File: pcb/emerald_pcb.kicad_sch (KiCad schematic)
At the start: 34 parts, among them J1 SIM_Card, J2 USB_B_Mini, J3 LiPoBatteryConnector, SW1 ESP RESET, U1 ESP32-S3-MINI-1U, U2 SIM800C, U3 SX1278, U4 MPU-6050, U5 FXMA108, U6 CH340N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

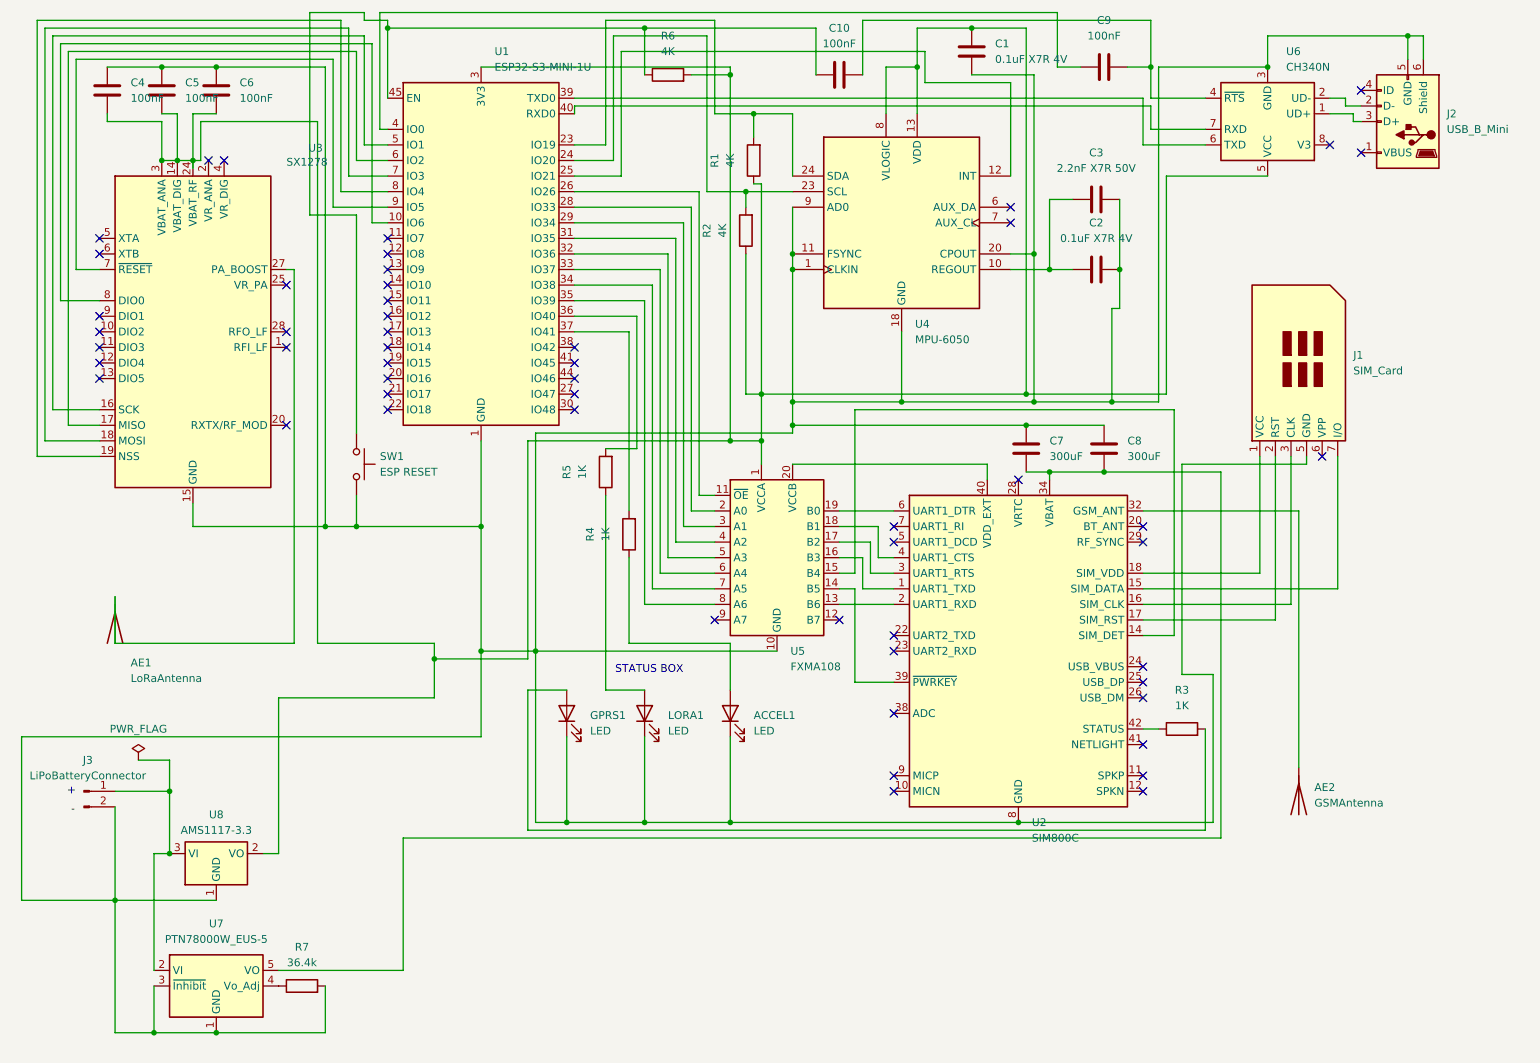
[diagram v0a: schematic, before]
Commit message: feat: update to version 1.1
Changed power inputs, various schematic changes, added decoupling capacitors, removed rare components
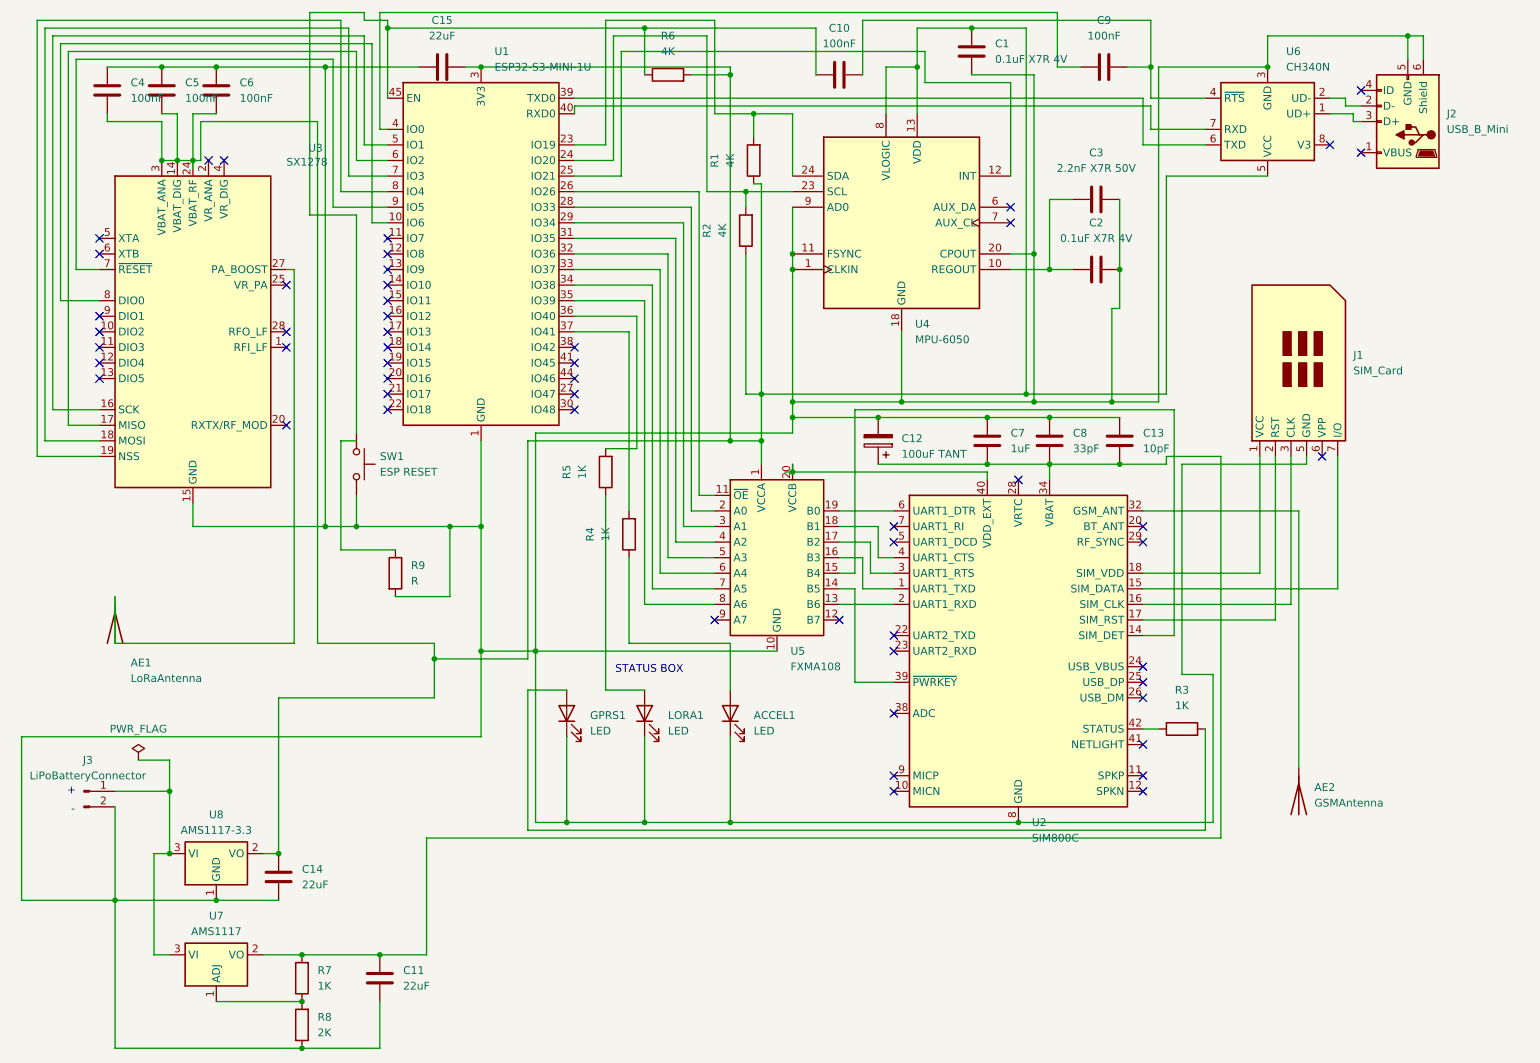
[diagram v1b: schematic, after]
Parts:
- removed U7: PTN78000W_EUS-5, Module:Texas_EUS_R-PDSS-T5_THT, symbol Converter_DCDC:PTN78000W_EUS-5
- added C11, C14, C15: 22uF, Capacitor_SMD:C_0201_0603Metric, symbol Device:C
- added C12: 100uF TANT, Capacitor_SMD:C_0201_0603Metric, symbol Device:C_Polarized
- added C13: 10pF, Capacitor_SMD:C_0201_0603Metric, symbol Device:C
- added R8: 2K, Resistor_SMD:R_0201_0603Metric, symbol Device:R
- added R9: R, symbol Device:R
- added U7: AMS1117, Package_TO_SOT_SMD:SOT-223-3_TabPin2, symbol Regulator_Linear:AMS1117
- C1, C2, C3: footprint Capacitor_SMD:CP_Elec_3x5.3 -> Capacitor_SMD:C_0201_0603Metric
- C10, C4, C5, C6, C9: footprint Capacitor_SMD:CP_Elec_4x3 -> Capacitor_SMD:C_0201_0603Metric
- C7: value 300uF -> 1uF; footprint Capacitor_SMD:CP_Elec_4x3 -> Capacitor_SMD:C_0201_0603Metric
- C8: value 300uF -> 33pF; footprint Capacitor_SMD:CP_Elec_4x3 -> Capacitor_SMD:C_0201_0603Metric
- R1, R2, R3, R4, R5, R6: footprint Resistor_SMD:R_0603_1608Metric -> Resistor_SMD:R_0201_0603Metric
- R7: value 36.4k -> 1K; footprint Resistor_SMD:R_0603_1608Metric -> Resistor_SMD:R_0201_0603Metric
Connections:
- net at C1.2, C4.1, C5.1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: now also C14.1, C15.2
- net at ACCEL1.1 (K), C1.1, C2.2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: now also C11.2, C12.2, C13.1, C14.2, C15.1, R8.1, R9.2; no longer R7.2
- net at C7.2, C8.2, U2.34 (VBAT)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: now also R7.2, C11.1, C12.1, C13.2, U7.2 (VO)
- net at R7.1: now also R8.2, U7.1 (ADJ)
- net at J3.1 (Pin_1), U8.3 (VI): now also U7.3 (VI)
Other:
- moved on the sheet: C7, C8

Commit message: feat: added pins to schem. fix: D+ and D- pins being assigned on ESP32
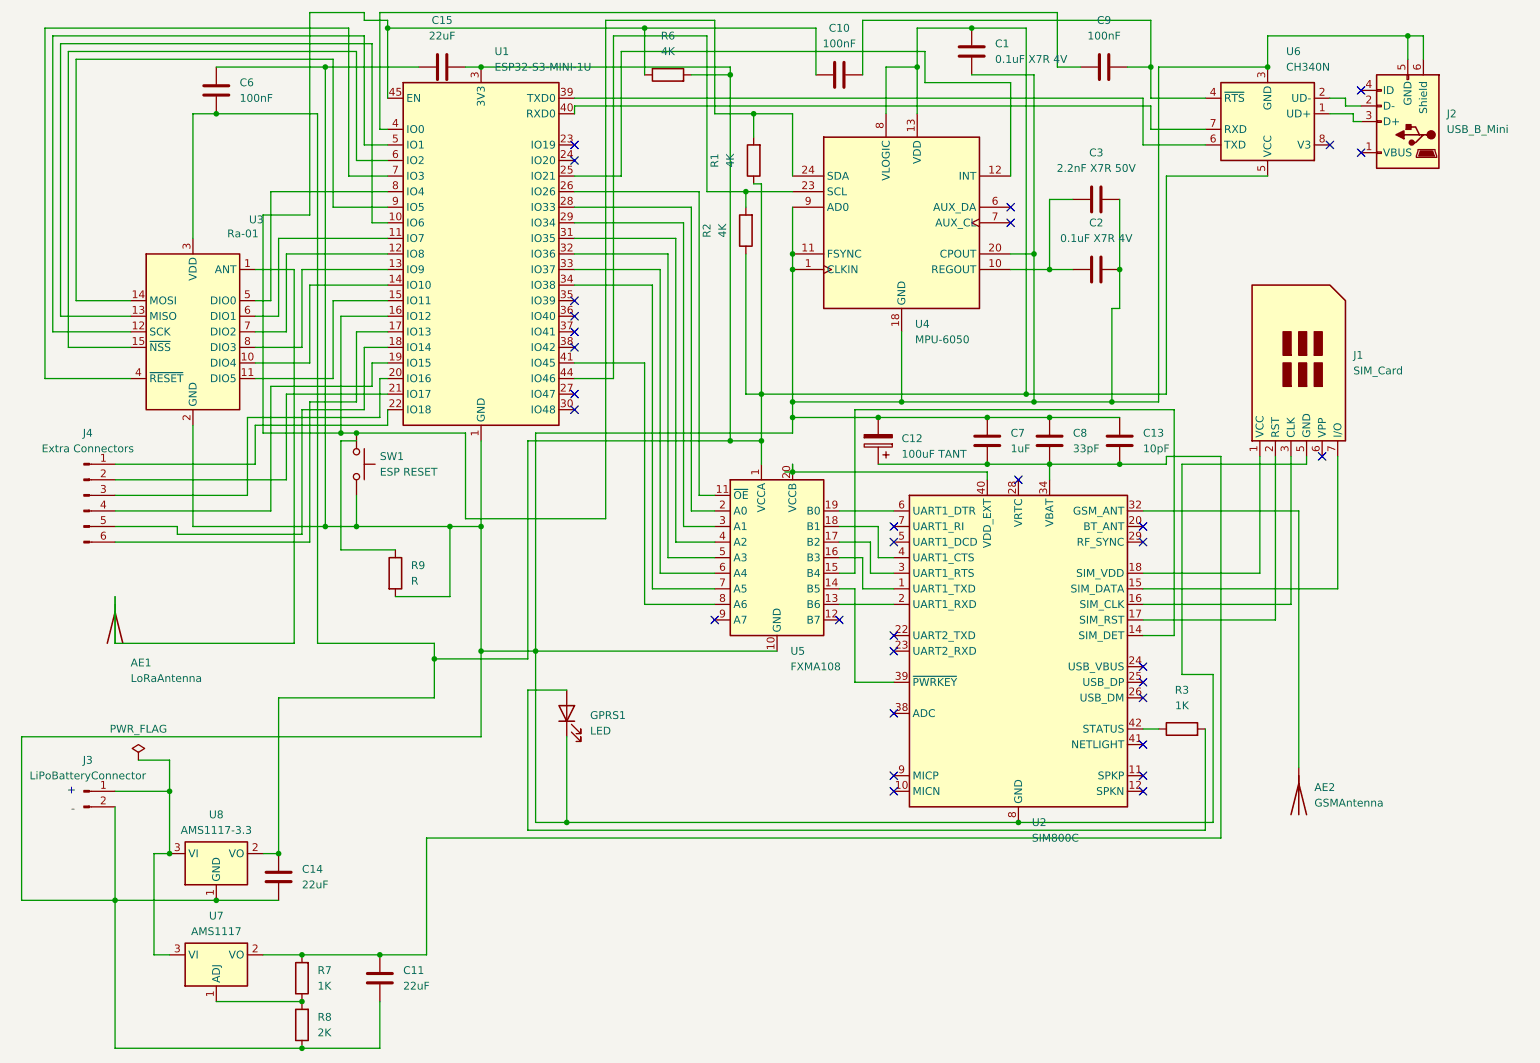
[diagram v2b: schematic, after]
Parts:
- removed ACCEL1, LORA1: LED, LED_SMD:LED_0201_0603Metric, symbol Device:LED
- removed C4, C5: 100nF, Capacitor_SMD:C_0201_0603Metric, symbol Device:C
- removed R4, R5: 1K, Resistor_SMD:R_0201_0603Metric, symbol Device:R
- added J4: Extra Connectors, symbol Connector:Conn_01x06_Pin
- U3: value SX1278 -> Ra-01; footprint Package_DFN_QFN:QFN-28-1EP_6x6mm_P0.65mm_EP4.8x4.8mm -> RF_Module:Ai-Thinker-Ra-01-LoRa; symbol RF:SX1278 -> RF_Module:Ai-Thinker-Ra-01
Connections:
- net at C1.1, C11.2, C12.2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: now also U3.16 (GND), U3.2 (GND), U3.9 (GND); no longer U3.15 (GND), U3.21 (GND), U3.22 (GND), U3.23 (GND), U3.26 (GND), U3.29 (GND)
- net at C1.2, C14.1, C15.2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: no longer U3.14 (VBAT_DIG), U3.24 (VBAT_RF)
- net at U5.8 (A6): now also U1.41 (IO45); no longer U1.35 (IO39)
- net at AE1.1 (A): now also U3.1 (ANT); no longer U3.27 (PA_BOOST)
- net at R1.2, U4.24 (SDA): now also C10.1, R6.1, SW1.1, U1.16 (IO12), U1.45 (EN); no longer U1.23 (IO19)
- net at R2.2, U4.23 (SCL): now also U1.44 (IO46); no longer U1.24 (IO20)
- net at U3.10 (DIO4): now also U1.14 (IO10)
- net at U3.11 (DIO5): now also U1.15 (IO11)
- net at U3.12 (SCK): now also U1.5 (IO1)
- net at U3.13 (MISO): now also U1.10 (IO6)
- net at U1.6 (IO2): now also U3.15 (~{NSS}); no longer U3.17 (MISO)
- net at U1.7 (IO3): now also U3.4 (~{RESET}); no longer U3.18 (MOSI)
- net at U1.8 (IO4): now also U3.5 (DIO0); no longer U3.19 (NSS)
- net at U3.6 (DIO1): now also U1.11 (IO7)
- net at U1.9 (IO5): now also U3.14 (MOSI); no longer U3.7 (~{RESET})
- net at U3.8 (DIO3): now also U1.13 (IO9); no longer U1.10 (IO6)
- net at U1.12 (IO8): now also U3.7 (DIO2)
- net at U1.17 (IO13): now also J4.6 (Pin_6)
- net at U1.18 (IO14): now also J4.5 (Pin_5)
- net at U1.19 (IO15): now also J4.4 (Pin_4)
- net at U1.20 (IO16): now also J4.3 (Pin_3)
- net at U1.21 (IO17): now also J4.2 (Pin_2)
- net at U1.22 (IO18): now also J4.1 (Pin_1)
- no-connect marks 54 -> 32
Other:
- note removed: "STATUS BOX"

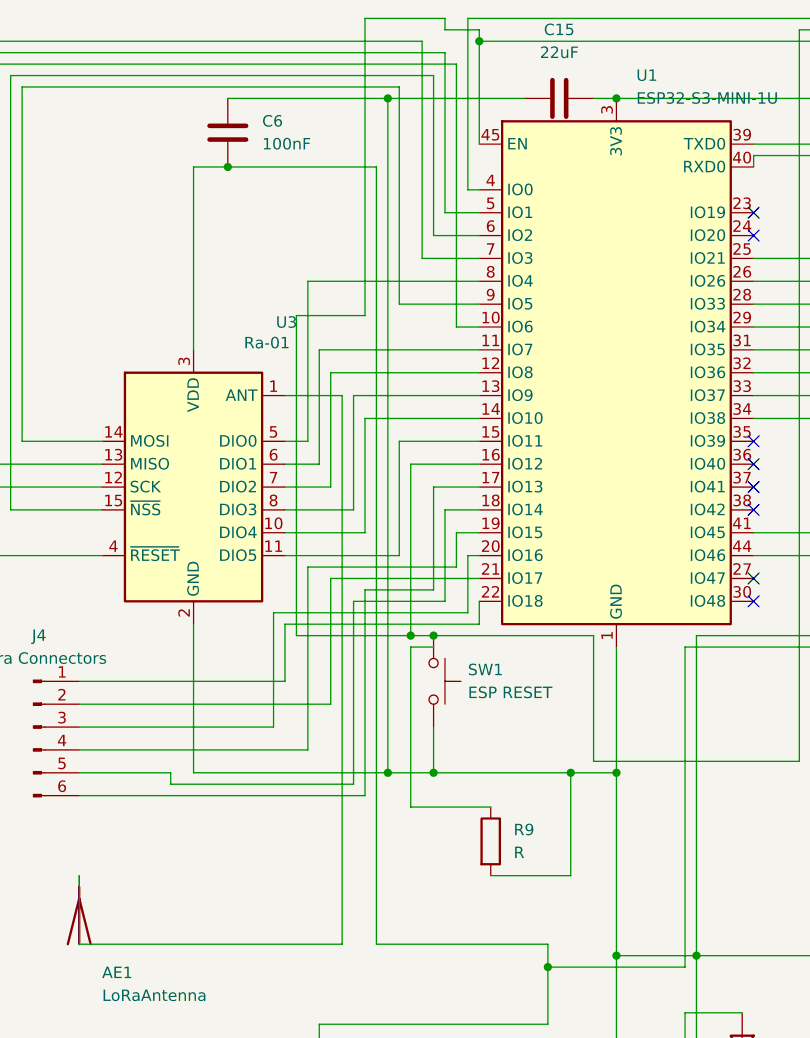
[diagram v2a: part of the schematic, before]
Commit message: feat: reroute for fewer vias, simplify design
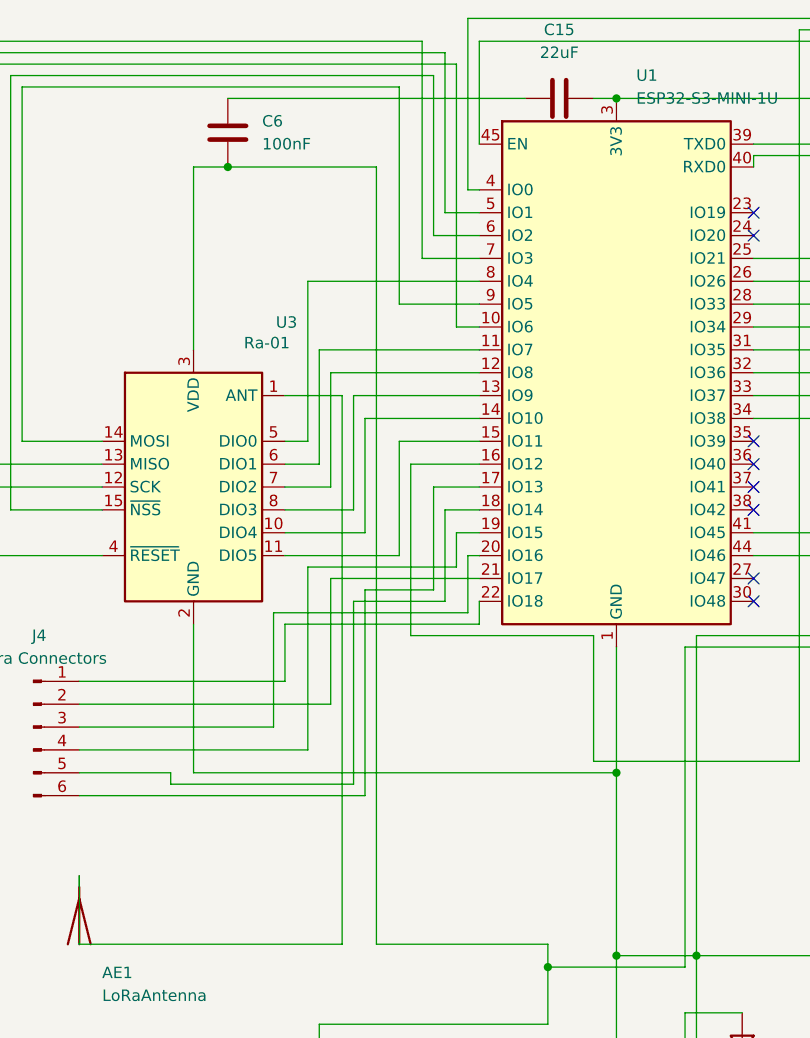
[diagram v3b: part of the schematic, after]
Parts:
- removed R9: R, symbol Device:R
- removed SW1: ESP RESET, Button_Switch_SMD:SW_DIP_SPSTx01_Slide_6.7x4.1mm_W6.73mm_P2.54mm_LowProfile_JPin, symbol Switch:SW_Push
- J3: footprint (none) -> Connector_AMASS:AMASS_XT30U-F_1x02_P5.0mm_Vertical
- J4: footprint (none) -> Connector_PinHeader_1.00mm:PinHeader_1x06_P1.00mm_Vertical
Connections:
- net at C1.1, C11.2, C12.2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: no longer C15.1, C6.2
- net at R1.2, U1.16 (IO12), U4.24 (SDA): no longer C10.1, R6.1, U1.45 (EN)
- new net: C15.1, C6.2
- new net: C10.1, R6.1, U1.45 (EN)
